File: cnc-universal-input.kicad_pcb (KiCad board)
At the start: 2 copper layers, 96.5 x 96.5 mm, 125 parts, among them J1 3PT, J10 2PT, J11 8PT, J12 USB_B_Mini, J13 2PT, J14 2PT, J2 3PT, J3 3PT, J4 3PT, J5 3PT, J6 3PT, J7 3PT, J8 3PT, J9 AVR-ISP-6, Q1 2N7002, Q11 2N7002, Q12 2N7002, Q13 2N7002, SW1 RESET, SW2 BTN, U1 ATmega328PB, U10 SFH617A-4, U11 SFH617A-4, U12 SFH617A-4, U13 SFH617A-4, U14 SFH617A-4, U15 SFH617A-4, U16 SFH617A-4, U18 CH340G, U19 TS2596S, U2 74HC595, U3 74HC595, U4 74HC595, U5 4051, U6 TS2596S, U8 LM7321, U9 SFH617A-4, Y1 18.432Mhz, Y2 12MHz

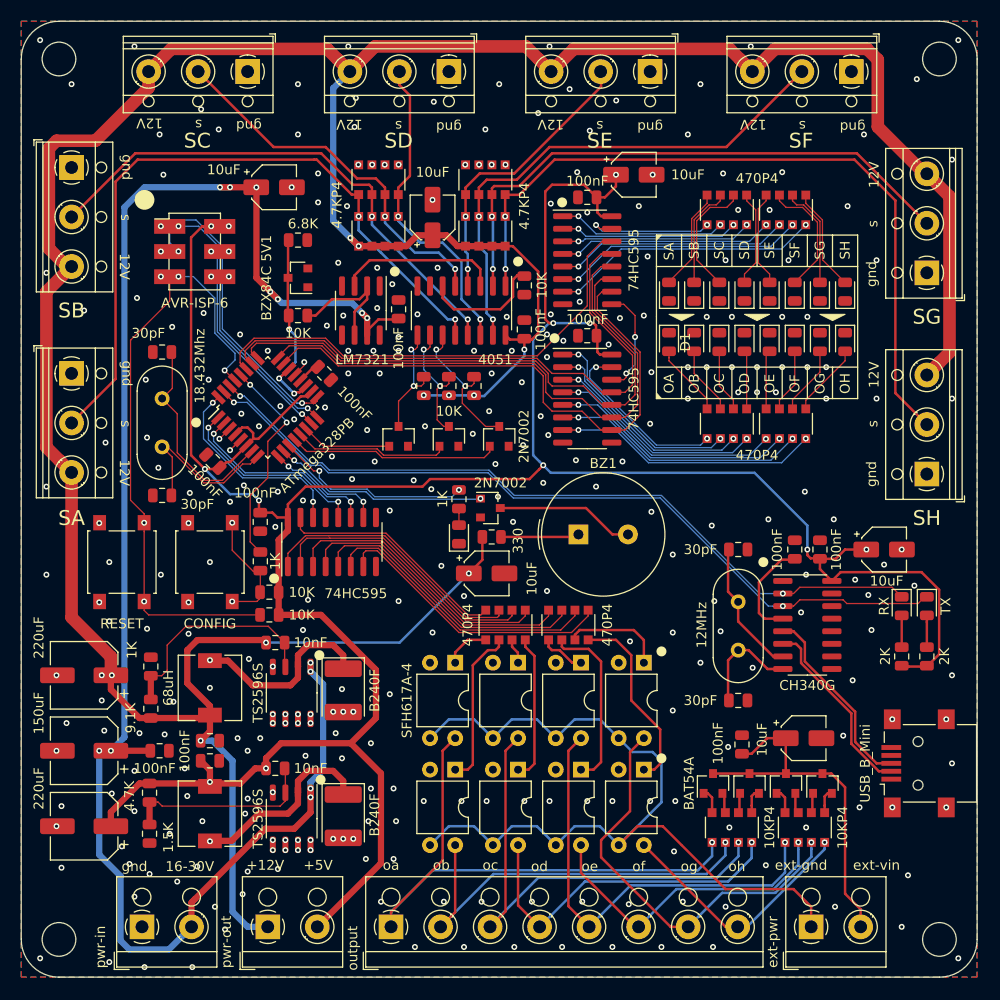
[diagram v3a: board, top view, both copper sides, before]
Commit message: crap!
wrong foot print
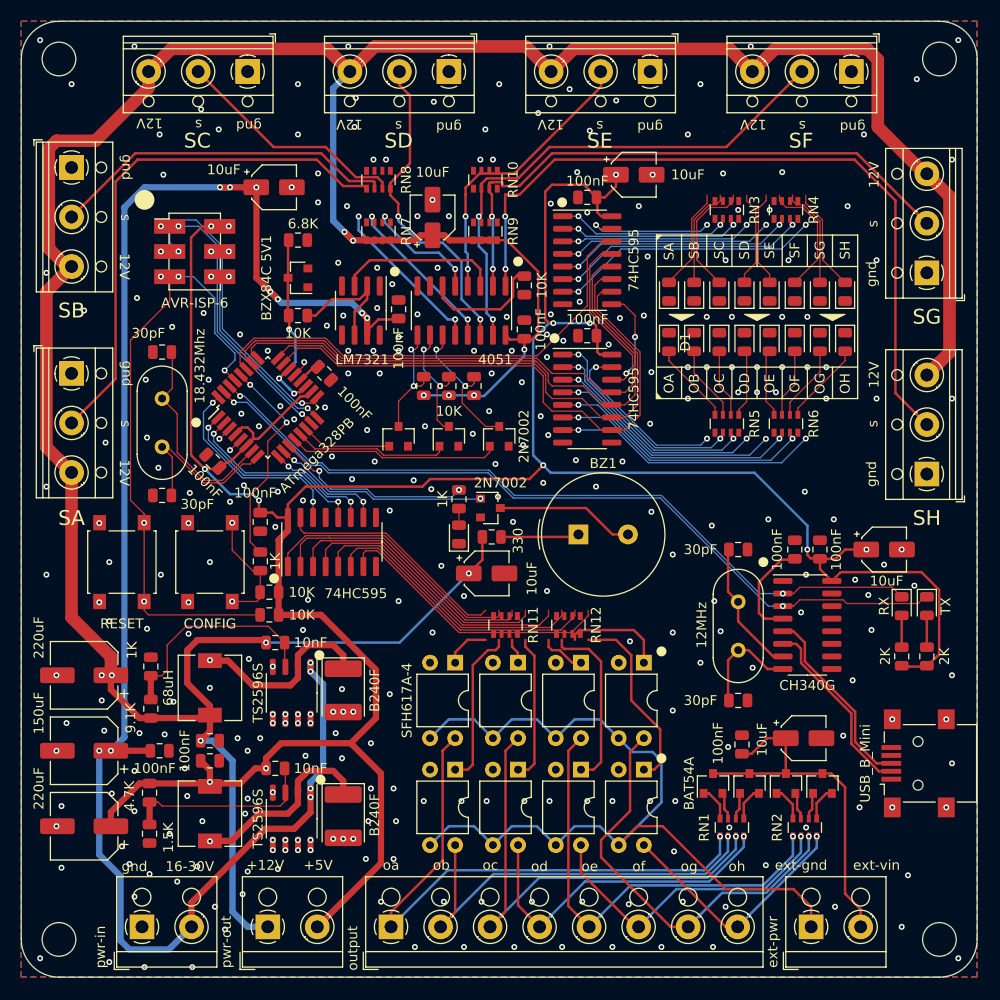
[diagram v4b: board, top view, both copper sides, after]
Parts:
- D1: footprint LED_SMD:LED_0805_2012Metric -> Diode_SMD:D_0805_2012Metric
- RN1, RN10, RN11, RN12, RN2, RN3, RN4, RN5, RN6, RN7, RN8, RN9: footprint Resistor_SMD:R_Array_Convex_4x1206 -> Resistor_SMD:R_Array_Convex_4x0603
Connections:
- J12 pad 1: (no net) -> Net-(J12-Pad1)
- J12 pad 4: (no net) -> Net-(J12-Pad4)
- U18 pad 10: (no net) -> Net-(U18-Pad10)
- U18 pad 11: (no net) -> Net-(U18-Pad11)
- U18 pad 12: (no net) -> Net-(U18-Pad12)
- U18 pad 13: (no net) -> Net-(U18-Pad13)
- U18 pad 14: (no net) -> Net-(U18-Pad14)
- U18 pad 15: (no net) -> Net-(U18-Pad15)
- U18 pad 9: (no net) -> Net-(U18-Pad9)
- U2 pad 9: (no net) -> Net-(U2-Pad9)
- U3 pad 9: (no net) -> Net-(U3-Pad9)
- U8 pad 1: (no net) -> Net-(U8-Pad1)
- U8 pad 5: (no net) -> Net-(U8-Pad5)
- U8 pad 8: (no net) -> Net-(U8-Pad8)
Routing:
- net /SC: track 38.0 -> 35.3 mm
- net /SB: track 53.4 -> 51.2 mm
- net /SA: track 71.8 -> 70.1 mm
- net /SG: track 58.2 -> 59.4 mm
- net Net-(D25-Pad2): track 2.50 -> 3.49 mm
- net Net-(D26-Pad1): track 2.55 -> 3.54 mm
- net Net-(D23-Pad1): track 2.55 -> 3.54 mm
- net Net-(D24-Pad2): track 2.51 -> 3.49 mm
- net Net-(D8-Pad2): track 7.46 -> 8.39 mm
- net Net-(D4-Pad2): track 5.91 -> 6.84 mm
- net Net-(D5-Pad2): track 5.96 -> 6.89 mm
- net Net-(D1-Pad2): track 7.32 -> 8.25 mm
- net /BD: track 35.0 -> 34.2 mm
- net Net-(D23-Pad2): track 2.07 -> 2.77 mm
- net Net-(D25-Pad1): track 2.01 -> 2.72 mm
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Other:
- board text added: "v1.4"
- board text removed: "v1.3"

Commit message: Update cnc-universal-input.kicad_pcb
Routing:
- net /SE: track 29.5 -> 34.4 mm
- net /SC: track 35.3 -> 40.0 mm
- net /SB: track 51.2 -> 55.6 mm
- net /SA: track 70.1 -> 74.1 mm
- net /SH: track 75.8 -> 79.0 mm
- net /SD: track 33.0 -> 34.7 mm
- net /SF: track 53.0 -> 54.7 mm
- net /OUT-D: track 27.9 -> 26.2 mm, vias 0 -> 2
- net Net-(RN3-Pad5): track 13.6 -> 15.2 mm
- net Net-(RN6-Pad5): track 23.9 -> 25.5 mm
- net Net-(RN4-Pad5): track 21.7 -> 23.3 mm
- net Net-(RN5-Pad5): track 18.0 -> 19.6 mm
- net /POH: track 19.1 -> 20.5 mm
- net /SG: track 59.4 -> 60.7 mm
- net Net-(RN6-Pad6): track 24.9 -> 26.0 mm
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
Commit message: fixed labels
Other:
- board text added: "+"
